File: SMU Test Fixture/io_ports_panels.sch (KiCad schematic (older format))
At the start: 27 parts, among them J10 Scope 1+, J11 Scope 2+, J12 Conn_01x03, J3 WG1, J4 WG2, J5 105-1102-001, J6 105-1102-001, J7 Scope 1-, J8 Scope 2-, J9 Ext. Source, K11 50 Ohm Ena, K12 Ext Meas Sel B, K13 Ext Meas Sel A, K14 Single/Diff Switch, K15 AC/DC Couple, K16 AC/DC Couple A

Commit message: Add footprints for low precision/low power parts.
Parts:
- R20, R21, R22, R23, R24, R25, R26: footprint (none) -> Resistor_SMD:R_0805_2012Metric_Pad1.20x1.40mm_HandSolder
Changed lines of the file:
@@
 F 0 "R20" V 1700 1875 50  0000 C CNN
 F 1 "49.9R" V 1850 1900 50  0000 C CNN
-F 2 "" H 1775 1875 50  0001 C CNN
+F 2 "Resistor_SMD:R_0805_2012Metric_Pad1.20x1.40mm_HandSolder" H 1775 1875 50  0001 C CNN
 F 3 "~" H 1775 1875 50  0001 C CNN
 	1    1775 1875
@@
 F 0 "R21" V 1700 2275 50  0000 C CNN
 F 1 "49.9R" V 1875 2300 50  0000 C CNN
-F 2 "" H 1775 2275 50  0001 C CNN
+F 2 "Resistor_SMD:R_0805_2012Metric_Pad1.20x1.40mm_HandSolder" H 1775 2275 50  0001 C CNN
 F 3 "~" H 1775 2275 50  0001 C CNN
 	1    1775 2275
@@
 F 0 "R25" H 8693 5746 50  0000 L CNN
 F 1 "27M" H 8693 5655 50  0000 L CNN
-F 2 "" H 8625 5700 50  0001 C CNN
+F 2 "Resistor_SMD:R_0805_2012Metric_Pad1.20x1.40mm_HandSolder" H 8625 5700 50  0001 C CNN
 F 3 "~" H 8625 5700 50  0001 C CNN
 	1    8625 5700
@@
 F 0 "R24" H 8450 5325 50  0000 L CNN
 F 1 "27M" H 8425 5250 50  0000 L CNN
-F 2 "" H 8625 5300 50  0001 C CNN
+F 2 "Resistor_SMD:R_0805_2012Metric_Pad1.20x1.40mm_HandSolder" H 8625 5300 50  0001 C CNN
 F 3 "~" H 8625 5300 50  0001 C CNN
 	1    8625 5300
@@
 F 0 "R26" V 8675 1950 50  0000 C CNN
 F 1 "49.9R" V 8850 1975 50  0000 C CNN
-F 2 "" H 8750 1950 50  0001 C CNN
+F 2 "Resistor_SMD:R_0805_2012Metric_Pad1.20x1.40mm_HandSolder" H 8750 1950 50  0001 C CNN
 F 3 "~" H 8750 1950 50  0001 C CNN
 	1    8750 1950
@@
 F 0 "R23" H 6593 2721 50  0000 L CNN
 F 1 "27M" H 6593 2630 50  0000 L CNN
-F 2 "" H 6525 2675 50  0001 C CNN
+F 2 "Resistor_SMD:R_0805_2012Metric_Pad1.20x1.40mm_HandSolder" H 6525 2675 50  0001 C CNN
 F 3 "~" H 6525 2675 50  0001 C CNN
 	1    6525 2675
@@
 F 0 "R22" H 6350 2300 50  0000 L CNN
 F 1 "27M" H 6325 2225 50  0000 L CNN
-F 2 "" H 6525 2275 50  0001 C CNN
+F 2 "Resistor_SMD:R_0805_2012Metric_Pad1.20x1.40mm_HandSolder" H 6525 2275 50  0001 C CNN
 F 3 "~" H 6525 2275 50  0001 C CNN
 	1    6525 2275

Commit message: More footprints added.
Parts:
- C18, C19, C20, C21: footprint (none) -> Capacitor_SMD:C_0805_2012Metric_Pad1.18x1.45mm_HandSolder
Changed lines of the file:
@@
 F 0 "C20" V 7246 5100 50  0000 C CNN
 F 1 "C_Small" V 7337 5100 50  0000 C CNN
-F 2 "" H 7475 5100 50  0001 C CNN
+F 2 "Capacitor_SMD:C_0805_2012Metric_Pad1.18x1.45mm_HandSolder" H 7475 5100 50  0001 C CNN
 F 3 "~" H 7475 5100 50  0001 C CNN
 	1    7475 5100
@@
 F 0 "C21" V 7246 5500 50  0000 C CNN
 F 1 "C_Small" V 7337 5500 50  0000 C CNN
-F 2 "" H 7475 5500 50  0001 C CNN
+F 2 "Capacitor_SMD:C_0805_2012Metric_Pad1.18x1.45mm_HandSolder" H 7475 5500 50  0001 C CNN
 F 3 "~" H 7475 5500 50  0001 C CNN
 	1    7475 5500
@@
 F 0 "C18" V 5146 2075 50  0000 C CNN
 F 1 "C_Small" V 5237 2075 50  0000 C CNN
-F 2 "" H 5375 2075 50  0001 C CNN
+F 2 "Capacitor_SMD:C_0805_2012Metric_Pad1.18x1.45mm_HandSolder" H 5375 2075 50  0001 C CNN
 F 3 "~" H 5375 2075 50  0001 C CNN
 	1    5375 2075
@@
 F 0 "C19" V 5146 2475 50  0000 C CNN
 F 1 "C_Small" V 5237 2475 50  0000 C CNN
-F 2 "" H 5375 2475 50  0001 C CNN
+F 2 "Capacitor_SMD:C_0805_2012Metric_Pad1.18x1.45mm_HandSolder" H 5375 2475 50  0001 C CNN
 F 3 "~" H 5375 2475 50  0001 C CNN
 	1    5375 2475

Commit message: Footprint updates
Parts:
- J3: PN (none) -> 5413969-2
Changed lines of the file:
@@
 F 2 "" H 3025 1900 50  0001 C CNN
 F 3 " ~" H 3025 1900 50  0001 C CNN
+F 4 "5413969-2" H 3025 1900 50  0001 C CNN "PN"
 	1    3025 1900
 	1    0    0    -1

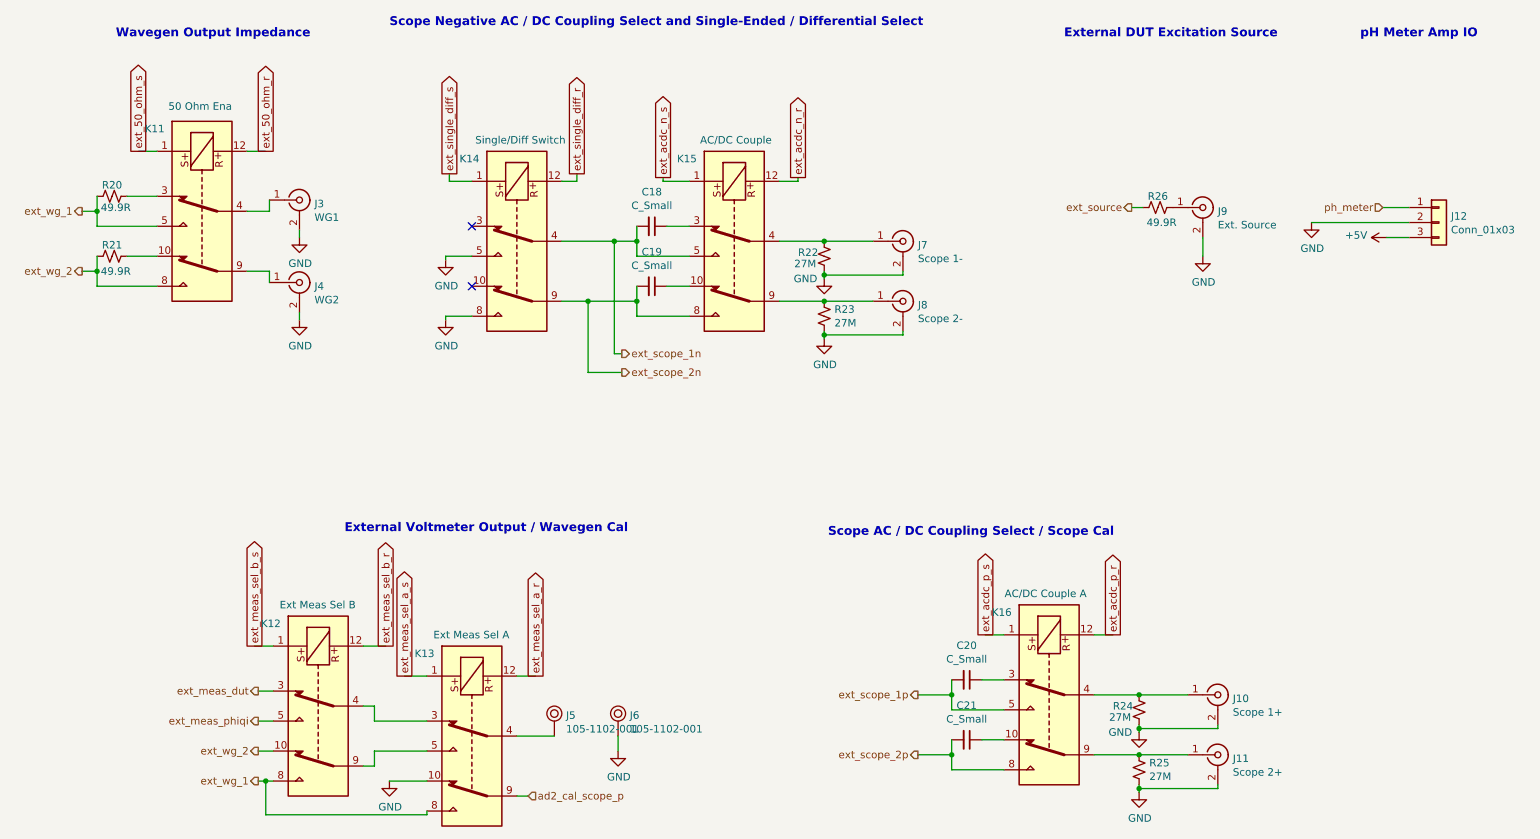
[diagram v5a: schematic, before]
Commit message: Switch to 28V txfrmr, nix preregs, nix 5V for AD2, switch to 12V relay power.
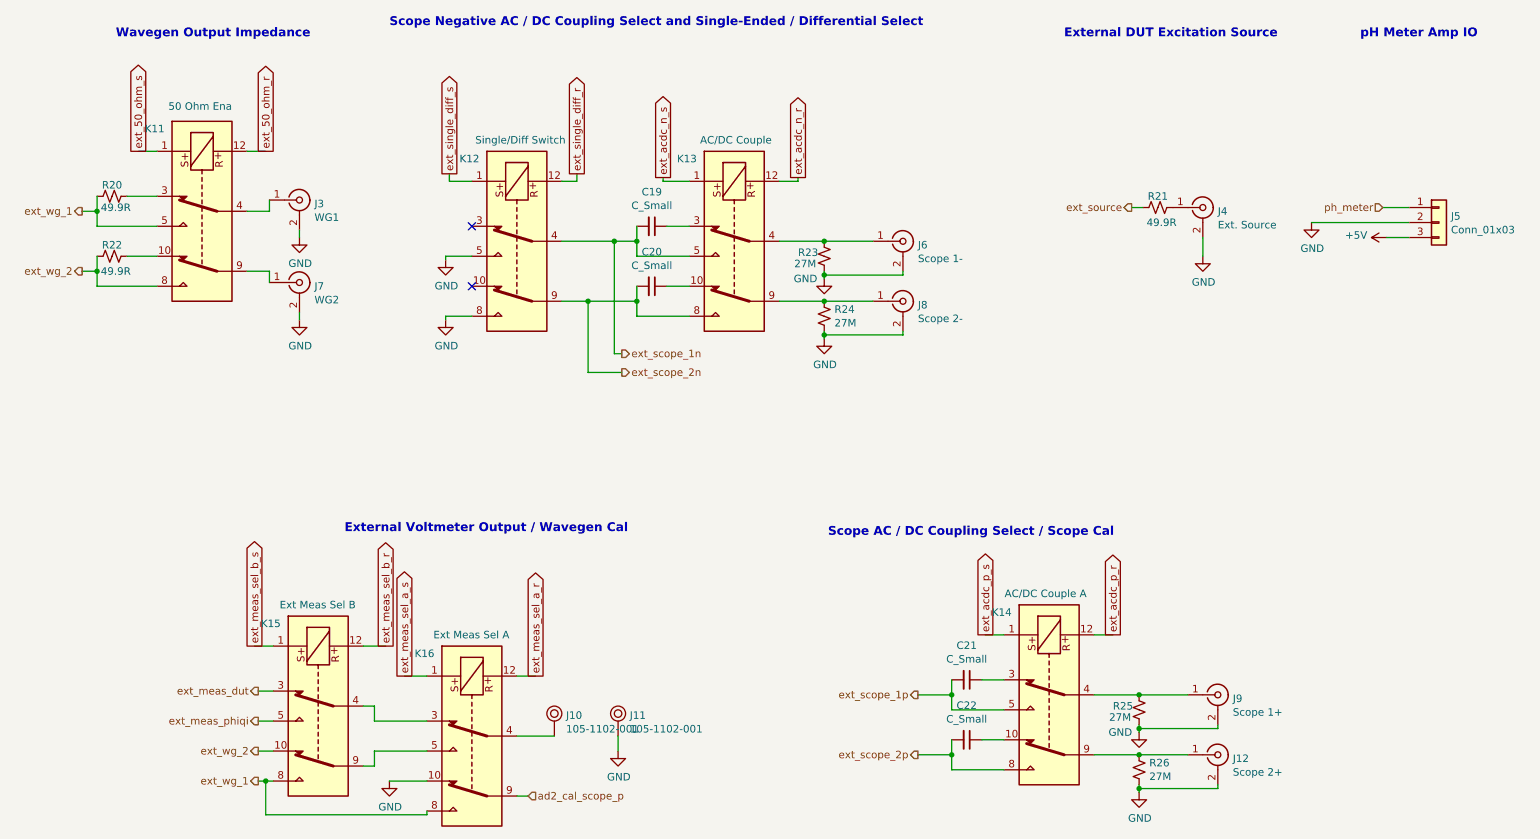
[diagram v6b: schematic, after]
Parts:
- renumbered C18 to C19, C19 to C20, C20 to C21, C21 to C22, J5 to J10, J6 to J11, J11 to J12, J9 to J4, J12 to J5, J7 to J6, J4 to J7, J10 to J9, K14 to K12, K15 to K13, K16 to K14, K12 to K15, K13 to K16, R26 to R21, R21 to R22, R22 to R23, R23 to R24, R24 to R25, R25 to R26
